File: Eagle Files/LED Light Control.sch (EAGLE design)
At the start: 9 parts, among them IC1 LM317MBSTT3

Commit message: Added plans for the board
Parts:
- removed X1: (no value), adafruit:ESP-12
- added C4: .01uF, adafruit:C-USC0805
- added JP1: (no value), adafruit:PINHD-1X6
- added PGM: (no value), switch-omron:10-XX
- added Q1: (no value), adafruit:MOSFET-NWAVE
- added R10, R9: 10K, adafruit:R-US_R0805
- added R3, R4, R5, R6: 10kΩ, adafruit:R-US_R0805
- added R7: 470Ω, adafruit:R-US_R0805
- added R8: 300Ω, adafruit:R-US_R0805
- added U1: (no value), esp8266modules:ESP12ESMD
- added X2: TERMINAL-BLOCK-3.5MM-2-PIN-ROUND-PAD, Rembrandt Electronics - Terminal Block 3-5mm v1-0:TERMINAL-BLOCK-3.5MM-2-PIN-ROUND-PAD
- added X3: TERMINAL-BLOCK-3.5MM-3-PIN-ROUND-PAD, Rembrandt Electronics - Terminal Block 3-5mm v1-0:TERMINAL-BLOCK-3.5MM-3-PIN-ROUND-PAD
- C1: value 0.1uF -> 1uF; device rcl:C-EU075-052X106 -> adafruit:C-USC0805
- C2: value 1uF -> 10uF; device resistor:CPOL-US085CS-1AR -> adafruit:C-USC0805
- C3: value 10uF -> 1000uF; device resistor:CPOL-US085CS-1AR -> adafruit:C-USC0805
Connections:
- removed net VIN: C1.1, D1.C, IC1.IN
- removed net VO: C2.+, D1.A, D2.C, IC1.OUT, R1.2
- new net +5V: C3.1, C4.1, D1.C, IC1.IN, R10.2, X2-1.K, X3-1.K
- new net 5VDATA: Q1.D, R10.1, R8.1
- new net DATA: Q1.S, R9.1, U1.GPIO4
- new net GPIO12: JP1.5, U1.GPIO12
- new net GPIO13: JP1.6, U1.GPIO13
- new net N$2: R3.2, U1.RESET
- new net N$3: R4.2, U1.CH_PD
- new net N$5: R6.1, U1.GPIO15
- new net N$6: PGM.P, R7.2
- new net N$7: R8.2, X3-2.K
- new net N$9: PGM.S, R5.1, U1.GPIO0
- new net RX: JP1.3, U1.RX
- new net TX: JP1.2, U1.TX
- new net VCC: C1.1, D1.A, D2.C, IC1.OUT, JP1.1, Q1.G, R1.2, R3.1, R4.1, R5.2, R9.2, U1.VCC
- net GND: now also C2.2, C3.2, C4.2, JP1.4, R6.2, R7.1, X2-2.K, X3-3.K; no longer C2.-, C3.-
- net N$1: now also C2.1; no longer C3.+
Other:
- note added: "(C)2018 Lehmancreations"
- note added: "Bi-directional Logic levil shifter 3.3v and 5v"
- note added: "LED Lighting Control"
- note added: "Licensed under the TAPR Open Hardware License: www.tapr.org/ohl"
- note added: "SKU: LED1"
- note added: "V0.0 (2018-08-06)"
- note added: "lehmancreations.com"
- note removed: "3V to 40V DC"
- moved on the sheet: C1, D1, D2, IC1, R1, R2

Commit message: Changes
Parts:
- removed X2: TERMINAL-BLOCK-3.5MM-2-PIN-ROUND-PAD, Rembrandt Electronics - Terminal Block 3-5mm v1-0:TERMINAL-BLOCK-3.5MM-2-PIN-ROUND-PAD
- added CN1: (no value), adafruit:DCBARRELPTH
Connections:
- net +5V: now also CN1.PWR; no longer X2-1.K
- net GND: now also CN1.GND; no longer X2-2.K
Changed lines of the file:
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@@
 <part name="C1" library="adafruit" deviceset="C-US" device="C0805" value="1uF"/>
 <part name="C2" library="adafruit" deviceset="C-US" device="C0805" value="10uF"/>
-<part name="X2" library="Rembrandt Electronics - Terminal Block 3-5mm v1-0" deviceset="TERMINAL-BLOCK-3.5MM-2-PIN" device="-ROUND-PAD"/>
 <part name="SUPPLY7" library="supply1" library_urn="urn:adsk.eagle:library:371" deviceset="GND" device=""/>
 <part name="X3" library="Rembrandt Electronics - Terminal Block 3-5mm v1-0" deviceset="TERMINAL-BLOCK-3.5MM-3-PIN" device="-ROUND-PAD"/>
@@
 <part name="P+9" library="supply1" library_urn="urn:adsk.eagle:library:371" deviceset="+5V" device=""/>
 <part name="U1" library="esp8266modules" deviceset="ESP12E" device="SMD"/>
+<part name="CN1" library="adafruit" deviceset="DCBARREL" device="PTH"/>
 </parts>
 <sheets>
@@
 <instance part="C1" gate="G$1" x="81.28" y="73.66"/>
 <instance part="C2" gate="G$1" x="66.04" y="66.04"/>
-<instance part="X2" gate="-1" x="12.7" y="152.4"/>
-<instance part="X2" gate="-2" x="12.7" y="139.7"/>
-<instance part="SUPPLY7" gate="1" x="5.08" y="139.7" rot="R270"/>
+<instance part="SUPPLY7" gate="1" x="58.42" y="142.24" rot="R90"/>
 <instance part="X3" gate="-1" x="127" y="149.86"/>
 <instance part="X3" gate="-2" x="127" y="142.24"/>
@@
 <instance part="R10" gate="G$1" x="170.18" y="58.42" rot="R90"/>
 <instance part="P+6" gate="VCC" x="157.48" y="54.864"/>
-<instance part="P+7" gate="1" x="10.16" y="144.78" rot="R180"/>
+<instance part="P+7" gate="1" x="48.26" y="157.48"/>
 <instance part="P+8" gate="1" x="12.7" y="93.98" rot="R90"/>
 <instance part="P+9" gate="1" x="170.18" y="68.58"/>
 <instance part="U1" gate="G$1" x="44.704" y="194.31"/>
+<instance part="CN1" gate="G$1" x="45.72" y="144.78"/>
 </instances>
 <busses>
@@
 <pinref part="SUPPLY5" gate="1" pin="GND"/>
 <wire x1="74.676" y1="186.69" x2="75.946" y2="186.69" width="0.1524" layer="91"/>
-</segment>
-<segment>
-<pinref part="SUPPLY7" gate="1" pin="GND"/>
-<pinref part="X2" gate="-2" pin="K"/>
-<wire x1="7.62" y1="139.7" x2="10.16" y2="139.7" width="0.1524" layer="91"/>
 </segment>
 <segment>
@@
 <pinref part="SUPPLY9" gate="1" pin="GND"/>
 <wire x1="165.1" y1="185.42" x2="147.32" y2="185.42" width="0.1524" layer="91"/>
+</segment>
+<segment>
+<pinref part="CN1" gate="G$1" pin="GND"/>
+<pinref part="SUPPLY7" gate="1" pin="GND"/>
+<wire x1="48.26" y1="142.24" x2="55.88" y2="142.24" width="0.1524" layer="91"/>
 </segment>
 </net>
@@
 <net name="+5V" class="0">
 <segment>
-<pinref part="X2" gate="-1" pin="K"/>
-<wire x1="10.16" y1="152.4" x2="10.16" y2="149.86" width="0.1524" layer="91"/>
-<pinref part="X3" gate="-1" pin="K"/>
-<wire x1="124.46" y1="149.86" x2="104.14" y2="149.86" width="0.1524" layer="91"/>
-<wire x1="104.14" y1="149.86" x2="88.9" y2="149.86" width="0.1524" layer="91"/>
-<wire x1="88.9" y1="149.86" x2="10.16" y2="149.86" width="0.1524" layer="91"/>
-<wire x1="10.16" y1="147.32" x2="10.16" y2="149.86" width="0.1524" layer="91"/>
-<junction x="10.16" y="149.86"/>
-<pinref part="P+7" gate="1" pin="+5V"/>
-<pinref part="C3" gate="G$1" pin="1"/>
-<wire x1="88.9" y1="144.78" x2="88.9" y2="149.86" width="0.1524" layer="91"/>
-<junction x="88.9" y="149.86"/>
-</segment>
-<segment>
 <pinref part="IC1" gate="G$1" pin="IN"/>
 <wire x1="25.4" y1="93.98" x2="22.86" y2="93.98" width="0.1524" layer="91"/>
@@
 <pinref part="P+9" gate="1" pin="+5V"/>
 </segment>
-</net>
+<segment>
+<pinref part="CN1" gate="G$1" pin="PWR"/>
+<pinref part="P+7" gate="1" pin="+5V"/>
+<wire x1="48.26" y1="147.32" x2="48.26" y2="152.4" width="0.1524" layer="91"/>
+<pinref part="X3" gate="-1" pin="K"/>
+<wire x1="48.26" y1="152.4" x2="48.26" y2="154.94" width="0.1524" layer="91"/>
+<wire x1="124.46" y1="149.86" x2="104.14" y2="149.86" width="0.1524" layer="91"/>
+<wire x1="104.14" y1="149.86" x2="88.9" y2="149.86" width="0.1524" layer="91"/>
+<pinref part="C3" gate="G$1" pin="1"/>
+<wire x1="88.9" y1="144.78" x2="88.9" y2="147.32" width="0.1524" layer="91"/>
+<wire x1="88.9" y1="147.32" x2="88.9" y2="149.86" width="0.1524" layer="91"/>
+<wire x1="48.26" y1="152.4" x2="88.9" y2="152.4" width="0.1524" layer="91"/>
+<wire x1="88.9" y1="152.4" x2="88.9" y2="147.32" width="0.1524" layer="91"/>
+<junction x="48.26" y="152.4"/>
+<junction x="88.9" y="147.32"/>
+</segment>
+</net>

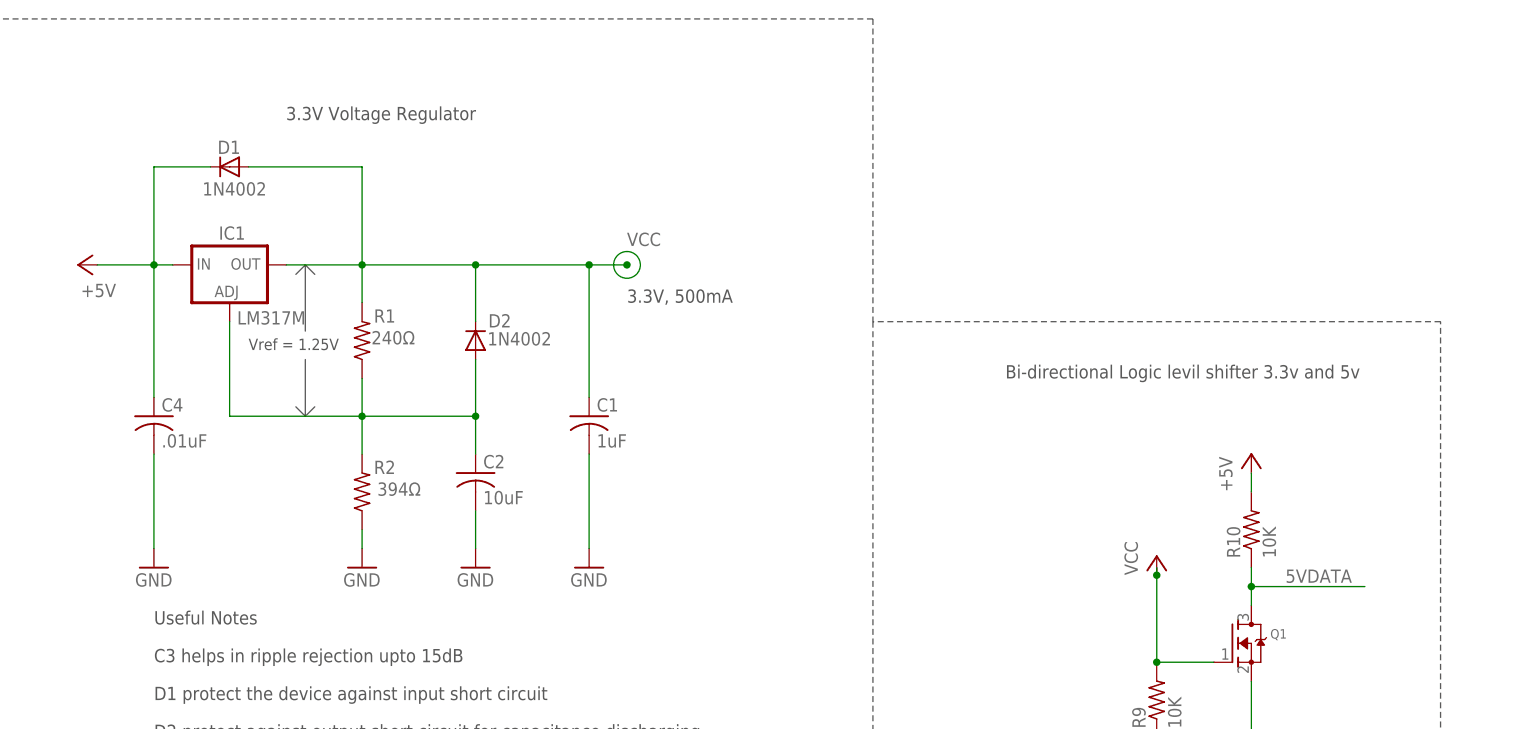
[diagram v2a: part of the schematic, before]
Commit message: Complete redisign of board. Also changed out the regulator on the schematic for a new one
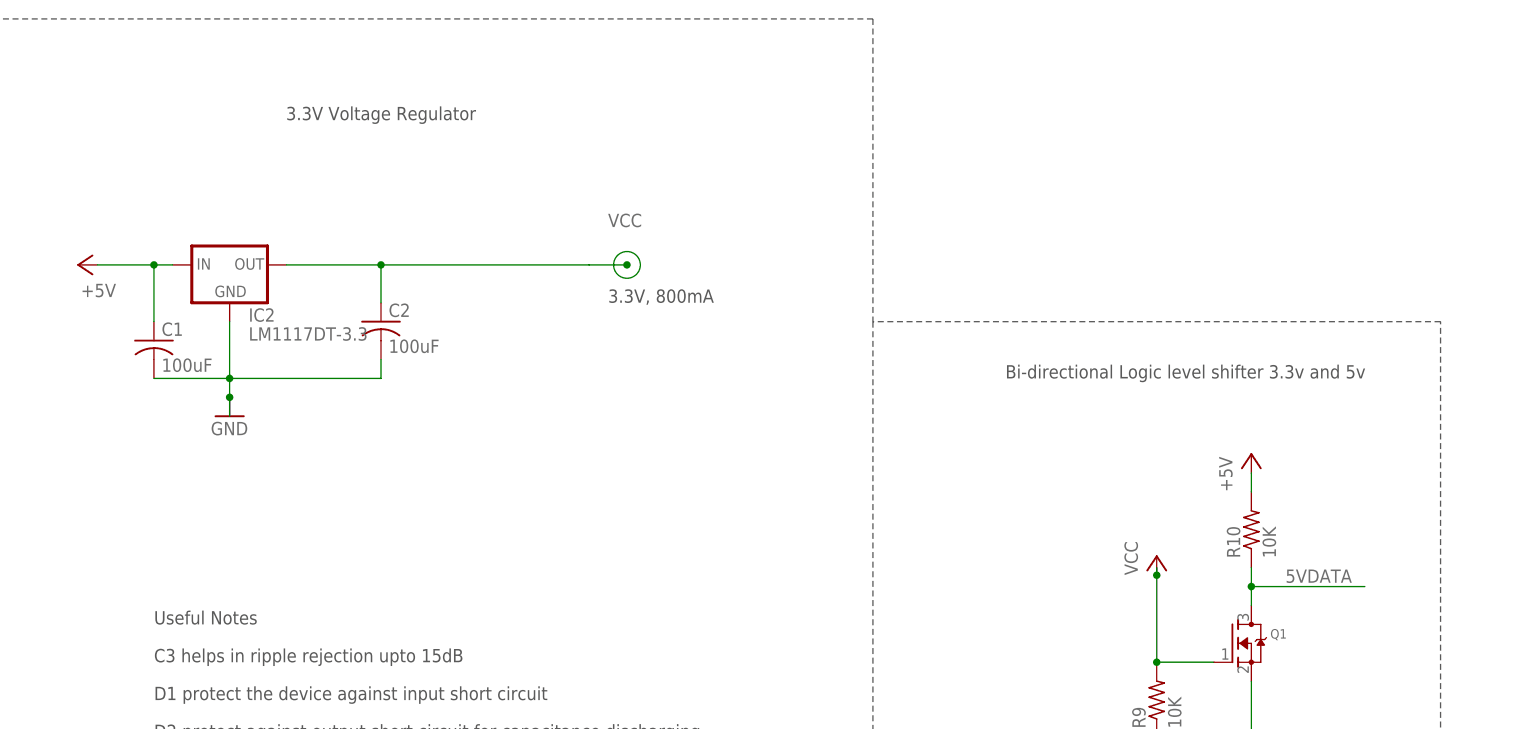
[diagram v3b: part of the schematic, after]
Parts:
- removed C4: .01uF, adafruit:C-USC0805
- removed D1, D2: 1N4002, diode:1N4004
- removed IC1: LM317MBSTT3, v-reg:LM317MBSTT3
- removed R1: 240Ω, resistor:R-US_M0805
- removed R2: 394Ω, resistor:R-US_M0805
- added IC2: LM1117DT-3.3, lm1117:LM1117DT-3.3
- C1: value 1uF -> 100uF
- C2: value 10uF -> 100uF
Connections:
- removed net N$1: C2.1, D2.A, IC1.ADJ, R1.1, R2.2
- net +5V: now also C1.1, IC2.IN; no longer C4.1, D1.C, IC1.IN
- net GND: now also IC2.GND; no longer C4.2, R2.1
- net VCC: now also C2.1, IC2.OUT; no longer C1.1, D1.A, D2.C, IC1.OUT, R1.2
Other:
- note added: "3.3V, 800mA"
- note added: "Bi-directional Logic level shifter 3.3v and 5v"
- note removed: "3.3V, 500mA"
- note removed: "Bi-directional Logic levil shifter 3.3v and 5v"
- note removed: "Vref = 1.25V"
- moved on the sheet: C1, C2

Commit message: Clean up Schematic
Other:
- note removed: "C2 of 1 µF tantalum capacitor on the output helps to improve transient response"
- note removed: "C3 helps in ripple rejection upto 15dB"
- note removed: "D1 protect the device against input short circuit"
- note removed: "D2 protect against output short circuit for capacitance discharging"
- note removed: "Useful Notes"
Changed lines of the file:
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@@
 <plain>
 <text x="53.34" y="114.3" size="1.778" layer="97" align="center">3.3V Voltage Regulator</text>
-<text x="22.86" y="40.64" size="1.778" layer="97">C3 helps in ripple rejection upto 15dB</text>
-<text x="22.86" y="35.56" size="1.778" layer="97">D1 protect the device against input short circuit</text>
-<text x="22.86" y="30.48" size="1.778" layer="97">D2 protect against output short circuit for capacitance discharging</text>
-<text x="22.86" y="25.4" size="1.778" layer="97">C2 of 1 µF tantalum capacitor on the output helps to improve transient response</text>
-<text x="22.86" y="45.72" size="1.778" layer="97">Useful Notes</text>
 <circle x="86.36" y="93.98" radius="1.79605" width="0.1524" layer="91"/>
 <text x="83.82" y="88.9" size="1.778" layer="97">3.3V, 800mA</text>

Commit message: Tied Ground pin on ESP12E to the GND
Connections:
- net GND: now also U1.GND

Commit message: Changed the size of the board to be smaller
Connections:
- net N$9 renamed GPIO0
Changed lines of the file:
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@@
 </segment>
 </net>
-<net name="N$9" class="0">
+<net name="GPIO0" class="0">
 <segment>
 <pinref part="R5" gate="G$1" pin="1"/>
